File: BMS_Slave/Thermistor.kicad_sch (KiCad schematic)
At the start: 5 parts, among them J1 Conn_01x01_Socket, J16 Conn_01x01_Socket

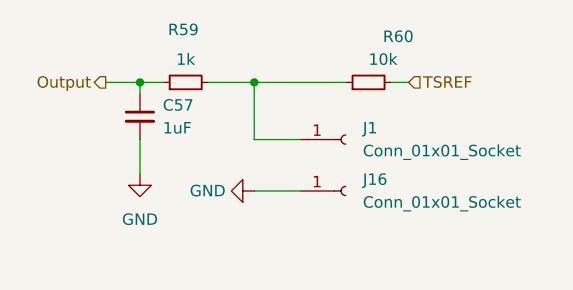
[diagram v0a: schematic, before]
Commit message: Dodano connectory hińskie zamiast padów, kontynuacja layoutu
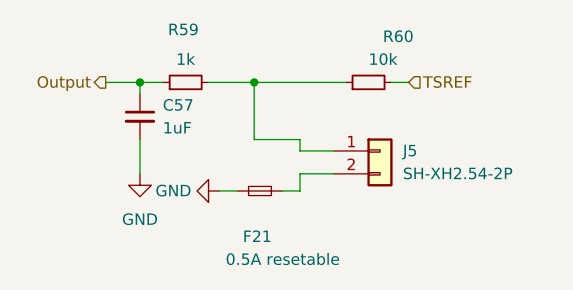
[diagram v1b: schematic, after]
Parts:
- removed J1, J16: Conn_01x01_Socket, Connector_Wire:SolderWirePad_1x01_SMD_2x4mm, symbol Connector:Conn_01x01_Socket
- added F21: 0.5A resetable, Fuse:Fuse_0805_2012Metric, symbol Device:Fuse_Small
- added J5: SH-XH2.54-2P, Connector_JST:JST_XH_B2B-XH-A_1x02_P2.50mm_Vertical, symbol Connector_Generic:Conn_01x02
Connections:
- net GND: now also F21.2
- net at R59.2, R60.1: now also J5.1 (Pin_1)
- new net: F21.1, J5.2 (Pin_2)

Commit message: Zostały małe poprawki na silkscreenie i otwory montażowe
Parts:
- removed F21: 0.5A resetable, Fuse:Fuse_0805_2012Metric, symbol Device:Fuse_Small
- removed J5: SH-XH2.54-2P, Connector_JST:JST_XH_B2B-XH-A_1x02_P2.50mm_Vertical, symbol Connector_Generic:Conn_01x02
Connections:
- net Thermistor: now reaches R59.2, R60.1
